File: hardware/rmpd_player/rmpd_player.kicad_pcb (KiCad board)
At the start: 2 copper layers, 108.6 x 69.2 mm, 117 parts, among them J1 POWER, J2 PROG, J3 LINE_OUT_INT_1, J4 LINE_OUT, J5 MICRO_SD, J6 POWER_INT, J7 LINE_OUT_INT_2, J8 RESERV, Q1 BC848, Q2 BC848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

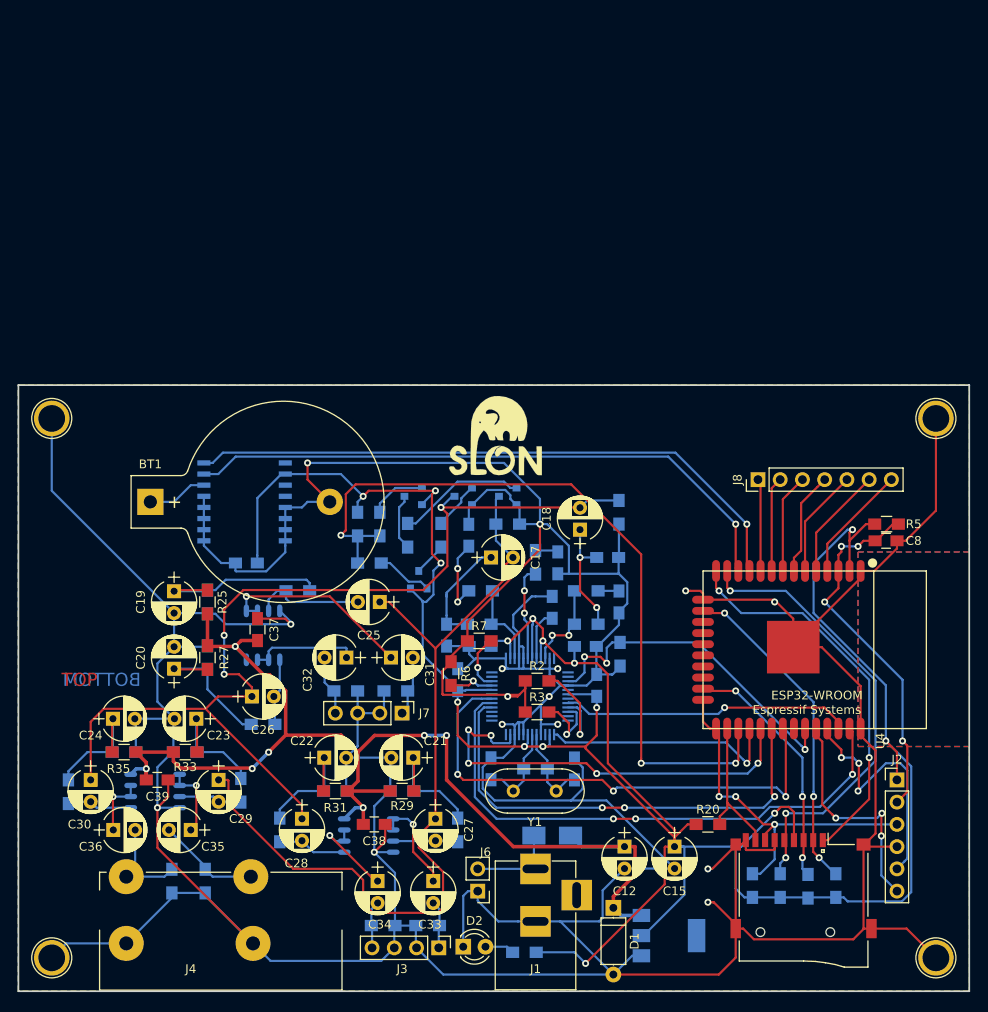
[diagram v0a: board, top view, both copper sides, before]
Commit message: smaller pcb
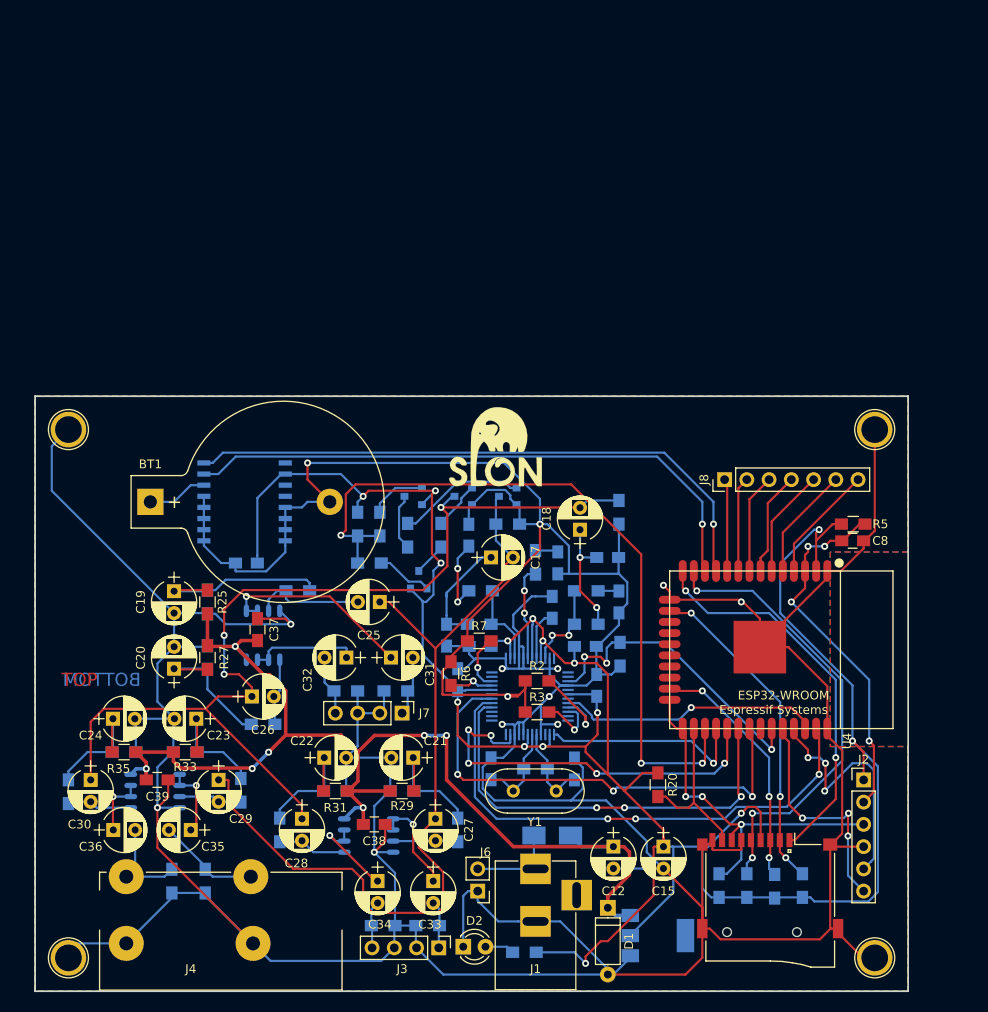
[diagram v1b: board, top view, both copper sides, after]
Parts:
- removed the REF** at (139.7, 76.2)
- removed the REF** at (139.7, 137.8)
- removed the REF** at (38.7, 76.2)
- added REF**: 1pin, Connectors:1pin, F.Cu at (132.7, 77.5)
- added REF**: 1pin, Connectors:1pin, F.Cu at (132.7, 137.8)
- added REF**: 1pin, Connectors:1pin, F.Cu at (40.6, 77.5)
- moved R20 7.29 mm to (108.0, 118.0), turned to 270 degrees
- moved R15 3.81 mm to (124.5, 129.5)
- moved C8 3.81 mm to (130.2, 90.2)
- moved J2 3.81 mm to (131.4, 117.5)
- moved J5 3.81 mm to (120.8, 134.9)
- moved J8 3.81 mm to (115.6, 83.2)
- moved R16 3.81 mm to (121.3, 129.6)
- moved R17 3.81 mm to (118.1, 129.5)
- moved R19 3.81 mm to (114.9, 129.5)
- moved R5 3.81 mm to (130.3, 88.3)
- moved U4 3.81 mm to (122.0, 102.6)
- moved REF** 1.91 mm to (40.6, 137.8)
- moved C15 1.27 mm to (108.6, 125.1)
- moved C12 1.27 mm to (102.9, 125.1)
- moved G*** 1.27 mm to (89.5, 79.4)
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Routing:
- net GND: track 706.3 -> 682.9 mm, vias 15 -> 13
- net VDD: track 314.8 -> 301.7 mm
- net VS_SI: track 63.8 -> 60.0 mm
- net VS_XCS: track 48.6 -> 44.8 mm
- net VS_SO: track 58.3 -> 54.5 mm
- net VS_SCLK: track 53.6 -> 49.8 mm
- net VS_XRESET: track 39.0 -> 35.2 mm
- net VS_XDCS: track 27.4 -> 23.6 mm
- net TRANSIENT_MUTE: track 88.7 -> 84.9 mm
- net VS_DREQ: track 33.2 -> 30.0 mm
- net 5V: track 137.2 -> 134.3 mm
- net Net-(R2-Pad2): track 12.4 -> 10.1 mm
- net I2C_SDA: track 70.2 -> 67.9 mm
- net I2C_SCL: track 71.3 -> 69.0 mm
- net SD_D1: track 17.4 -> 19.4 mm
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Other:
- board size 108.6 x 69.2 mm -> 99.7 x 67.9 mm

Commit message: better vdd route to ds3231
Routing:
- net VDD: track 301.7 -> 352.5 mm, vias 15 -> 17
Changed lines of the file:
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@@
-(kicad_pcb (version 20171130) (host pcbnew 5.0.1-5.0.1)
+(kicad_pcb (version 20171130) (host pcbnew 5.0.2-5.0.2)
   (general
     (thickness 1.6)
     (drawings 10)
-    (tracks 1084)
+    (tracks 1091)
     (zones 0)
     (modules 117)
@@
   (segment (start 128.905 88.265) (end 127.905 88.265) (width 0.25) (layer F.Cu) (net 5) (status 10))
   (segment (start 129.005 88.265) (end 128.905 88.265) (width 0.25) (layer F.Cu) (net 5) (status 30))
-  (segment (start 71.755 82.55) (end 74.295 85.09) (width 0.25) (layer B.Cu) (net 5))
   (segment (start 65.405 82.55) (end 71.755 82.55) (width 0.25) (layer B.Cu) (net 5) (status 10))
   (segment (start 114.035 130.89) (end 113.03 129.885) (width 0.25) (layer B.Cu) (net 5))
@@
   (segment (start 101.061501 112.298499) (end 101.061501 110.369868) (width 0.25) (layer F.Cu) (net 5))
   (segment (start 100.965 109.707682) (end 101.061501 109.804183) (width 0.25) (layer B.Cu) (net 5))
+  (via (at 89.535 82.55) (size 0.8) (drill 0.4) (layers F.Cu B.Cu) (net 5))
+  (segment (start 71.755 82.55) (end 89.535 82.55) (width 0.25) (layer B.Cu) (net 5))
+  (via (at 93.98 82.55) (size 0.8) (drill 0.4) (layers F.Cu B.Cu) (net 5))
+  (segment (start 89.535 82.55) (end 93.98 82.55) (width 0.25) (layer F.Cu) (net 5))
+  (segment (start 102.475002 82.55) (end 112.635002 92.71) (width 0.25) (layer B.Cu) (net 5))
+  (segment (start 93.98 82.55) (end 102.475002 82.55) (width 0.25) (layer B.Cu) (net 5))
+  (segment (start 121.850685 92.71) (end 121.92 92.779315) (width 0.25) (layer B.Cu) (net 5))
+  (segment (start 112.635002 92.71) (end 121.850685 92.71) (width 0.25) (layer B.Cu) (net 5))
   (segment (start 129.07 90.17) (end 128.945 90.17) (width 0.25) (layer F.Cu) (net 6) (status 30))
   (segment (start 130.975 88.265) (end 129.07 90.17) (width 0.25) (layer F.Cu) (net 6) (status 30))
@@
     (connect_pads (clearance 0.508))
     (min_thickness 0.254)
-    (fill (arc_segments 16) (thermal_gap 0.508) (thermal_bridge_width 0.508))
+    (fill yes (arc_segments 16) (thermal_gap 0.508) (thermal_bridge_width 0.508))
     (polygon
       (pts
@@
     (connect_pads (clearance 0.508))
     (min_thickness 0.254)
-    (fill (arc_segments 16) (thermal_gap 0.508) (thermal_bridge_width 0.508))
+    (fill yes (arc_segments 16) (thermal_gap 0.508) (thermal_bridge_width 0.508))
     (polygon
       (pts

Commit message: wip: volume control
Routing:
- net VDD: track 352.5 -> 354.7 mm
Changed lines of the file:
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@@
     (thickness 1.6)
     (drawings 10)
-    (tracks 1091)
+    (tracks 1096)
     (zones 0)
     (modules 117)
@@
   (segment (start 107.459999 125.170001) (end 107.535 125.095) (width 0.25) (layer F.Cu) (net 5))
   (segment (start 107.459999 130.665001) (end 107.459999 125.170001) (width 0.25) (layer F.Cu) (net 5))
-  (segment (start 109.710001 125.170001) (end 109.635 125.095) (width 0.25) (layer B.Cu) (net 5))
-  (segment (start 109.710001 130.319999) (end 109.710001 125.170001) (width 0.25) (layer B.Cu) (net 5))
-  (segment (start 109.635 125.095) (end 108.585 125.095) (width 0.25) (layer B.Cu) (net 5))
+  (segment (start 109.635 125.095) (end 108.585 125.095) (width 0.6) (layer B.Cu) (net 5))
   (segment (start 105.05 135.255) (end 105.05 134.98) (width 0.25) (layer B.Cu) (net 5))
-  (segment (start 105.05 134.98) (end 109.710001 130.319999) (width 0.25) (layer B.Cu) (net 5))
   (segment (start 99.695 114.3) (end 102.235 116.84) (width 0.25) (layer F.Cu) (net 5))
   (segment (start 99.695 113.665) (end 99.695 114.3) (width 0.25) (layer F.Cu) (net 5))
@@
   (segment (start 102.235 116.84) (end 104.14 118.745) (width 0.25) (layer F.Cu) (net 5))
   (segment (start 104.14 118.745) (end 108.585 123.19) (width 0.25) (layer F.Cu) (net 5))
-  (segment (start 113.03 125.095) (end 109.635 125.095) (width 0.25) (layer B.Cu) (net 5))
   (segment (start 101.061501 110.369868) (end 101.061501 109.804183) (width 0.25) (layer F.Cu) (net 5))
   (segment (start 99.695 113.665) (end 101.061501 112.298499) (width 0.25) (layer F.Cu) (net 5))
@@
   (segment (start 121.850685 92.71) (end 121.92 92.779315) (width 0.25) (layer B.Cu) (net 5))
   (segment (start 112.635002 92.71) (end 121.850685 92.71) (width 0.25) (layer B.Cu) (net 5))
+  (segment (start 104.8 135.255) (end 105.05 135.255) (width 0.25) (layer B.Cu) (net 5))
+  (segment (start 105.05 135.255) (end 107.315 135.255) (width 0.6) (layer B.Cu) (net 5))
+  (segment (start 107.315 135.255) (end 109.22 133.35) (width 0.6) (layer B.Cu) (net 5))
+  (segment (start 109.22 133.35) (end 109.22 131.445) (width 0.6) (layer B.Cu) (net 5))
+  (segment (start 109.22 131.445) (end 110.49 130.175) (width 0.6) (layer B.Cu) (net 5))
+  (segment (start 110.49 130.175) (end 110.49 125.95) (width 0.6) (layer B.Cu) (net 5))
+  (segment (start 110.49 125.95) (end 110.49 125.095) (width 0.6) (layer B.Cu) (net 5))
+  (segment (start 113.03 125.095) (end 110.49 125.095) (width 0.25) (layer B.Cu) (net 5))
+  (segment (start 110.49 125.095) (end 109.635 125.095) (width 0.6) (layer B.Cu) (net 5))
   (segment (start 129.07 90.17) (end 128.945 90.17) (width 0.25) (layer F.Cu) (net 6) (status 30))
   (segment (start 130.975 88.265) (end 129.07 90.17) (width 0.25) (layer F.Cu) (net 6) (status 30))
@@
   (segment (start 87.85 92.075) (end 83.82 96.105) (width 0.25) (layer B.Cu) (net 12))
   (segment (start 93.795 127.45) (end 93.98 127.635) (width 0.25) (layer B.Cu) (net 13) (status 30))
-  (segment (start 93.795 123.825) (end 93.795 127.45) (width 0.25) (layer B.Cu) (net 13) (status 30))
-  (segment (start 87.376 127.635) (end 93.98 127.635) (width 0.25) (layer B.Cu) (net 13))
+  (segment (start 93.795 123.825) (end 93.795 127.45) (width 0.8) (layer B.Cu) (net 13) (status 30))
+  (segment (start 87.376 127.635) (end 93.98 127.635) (width 0.8) (layer B.Cu) (net 13))
   (via (at 124.46 121.83) (size 0.8) (drill 0.4) (layers F.Cu B.Cu) (net 14))
   (via (at 129.660748 123.877066) (size 0.8) (drill 0.4) (layers F.Cu B.Cu) (net 14))
@@
   (segment (start 81.28 112.395) (end 83.82 112.395) (width 0.4) (layer B.Cu) (net 55))
   (via (at 83.82 112.395) (size 0.8) (drill 0.4) (layers F.Cu B.Cu) (net 55))
-  (segment (start 103.11 132.955) (end 102.235 132.08) (width 0.4) (layer B.Cu) (net 55))
-  (segment (start 104.8 132.955) (end 103.11 132.955) (width 0.4) (layer B.Cu) (net 55))
-  (segment (start 102.235 130.78) (end 102.235 132.08) (width 0.4) (layer F.Cu) (net 55))
-  (segment (start 104.705001 128.309999) (end 102.235 130.78) (width 0.4) (layer F.Cu) (net 55))
-  (segment (start 104.07 125.095) (end 102.87 125.095) (width 0.4) (layer F.Cu) (net 55))
-  (segment (start 104.705001 125.730001) (end 104.07 125.095) (width 0.4) (layer F.Cu) (net 55))
-  (segment (start 104.705001 128.309999) (end 104.705001 125.730001) (width 0.4) (layer F.Cu) (net 55))
+  (segment (start 103.11 132.955) (end 102.235 132.08) (width 0.8) (layer B.Cu) (net 55))
+  (segment (start 104.8 132.955) (end 103.11 132.955) (width 0.8) (layer B.Cu) (net 55))
+  (segment (start 102.235 130.78) (end 102.235 132.08) (width 0.8) (layer F.Cu) (net 55))
+  (segment (start 104.705001 128.309999) (end 102.235 130.78) (width 0.8) (layer F.Cu) (net 55))
+  (segment (start 104.07 125.095) (end 102.87 125.095) (width 0.8) (layer F.Cu) (net 55))
+  (segment (start 104.705001 125.730001) (end 104.07 125.095) (width 0.8) (layer F.Cu) (net 55))
+  (segment (start 104.705001 128.309999) (end 104.705001 125.730001) (width 0.8) (layer F.Cu) (net 55))
   (segment (start 91.44 125.095) (end 102.87 125.095) (width 0.4) (layer F.Cu) (net 55))
   (segment (start 83.82 112.395) (end 83.82 117.475) (width 0.4) (layer F.Cu) (net 55))
   (segment (start 83.82 117.475) (end 91.44 125.095) (width 0.4) (layer F.Cu) (net 55))
-  (segment (start 99.245 125.095) (end 97.975 123.825) (width 0.4) (layer B.Cu) (net 55))
-  (segment (start 102.87 125.095) (end 99.245 125.095) (width 0.4) (layer B.Cu) (net 55))
+  (segment (start 99.245 125.095) (end 97.975 123.825) (width 0.8) (layer B.Cu) (net 55))
+  (segment (start 102.87 125.095) (end 99.245 125.095) (width 0.8) (layer B.Cu) (net 55))
   (segment (start 82.55 121.92) (end 82.55 102.455) (width 0.25) (layer F.Cu) (net 56) (status 10))
   (segment (start 89.495 88.305) (end 89.455 88.265) (width 0.25) (layer B.Cu) (net 56) (status 30))
@@
     (connect_pads (clearance 0.508))
     (min_thickness 0.254)
-    (fill yes (arc_segments 16) (thermal_gap 0.508) (thermal_bridge_width 0.508))
+    (fill (arc_segments 16) (thermal_gap 0.508) (thermal_bridge_width 0.508))
     (polygon
       (pts
@@
     (connect_pads (clearance 0.508))
     (min_thickness 0.254)
-    (fill yes (arc_segments 16) (thermal_gap 0.508) (thermal_bridge_width 0.508))
+    (fill (arc_segments 16) (thermal_gap 0.508) (thermal_bridge_width 0.508))
     (polygon
       (pts

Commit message: wip: new tps54331 power
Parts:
- added C40: 1000pF, Capacitors_SMD:C_0805_HandSoldering, F.Cu at (107.9, 139.1)
- added C41: 1000pF, Capacitors_SMD:C_0805_HandSoldering, F.Cu at (113.7, 43.4)
- added C42: 10.0, Capacitors_THT:CP_Radial_D5.0mm_P2.50mm, F.Cu at (101.6, 123.8)
- added C43: 10.0, Capacitors_THT:CP_Radial_D5.0mm_P2.50mm, F.Cu at (95.0, 35.3)
- added C44: 47pF, Capacitors_SMD:C_0805_HandSoldering, B.Cu at (111.8, 139.1)
- added C45: 47pF, Capacitors_SMD:C_0805_HandSoldering, F.Cu at (111.9, 45.9)
- added C46: 0.01, Capacitors_SMD:C_0805_HandSoldering, B.Cu at (109.2, 127.0)
- added C47: 0.01, Capacitors_SMD:C_0805_HandSoldering, F.Cu at (111.9, 47.7)
- added C48: 100n, Capacitors_SMD:C_0805_HandSoldering, F.Cu at (100.3, 135.3)
- added C49: 100n, Capacitors_SMD:C_0805_HandSoldering, F.Cu at (111.9, 49.5)
- added C50: 47uF, Capacitors_SMD:C_1206_HandSoldering, B.Cu at (116.1, 137.2)
- added C51: 47uF, Capacitors_SMD:C_1206_HandSoldering, F.Cu at (101.6, 48.2)
- added C52: 47uF, Capacitors_SMD:C_1206_HandSoldering, B.Cu at (122.5, 137.2)
- added C53: 47uF, Capacitors_SMD:C_1206_HandSoldering, F.Cu at (108.2, 43.9)
- added D3: B340, Opto-Devices:PhotoDiode_SMD-DIL2_4.5x4, F.Cu at (120.7, 37.5)
- added L1: 6.8uH, Inductors_SMD:L_6.3x6.3_H3, F.Cu at (104.8, 134.0)
- added L2: 6.8uH, Inductors_SMD:L_6.3x6.3_H3, F.Cu at (94.6, 44.1)
- added R50: 30k, Resistors_SMD:R_0805_HandSoldering, F.Cu at (102.9, 139.1)
- added R51: 30k, Resistors_SMD:R_0805_HandSoldering, F.Cu at (100.7, 52.1)
- added R52: 15k, Resistors_SMD:R_0805_HandSoldering, F.Cu at (111.1, 129.5)
- added R53: 4k7, Resistors_SMD:R_0805_HandSoldering, B.Cu at (111.1, 132.7)
- added R54: 10k, Resistors_SMD:R_0805_HandSoldering, F.Cu at (113.8, 41.6)
- added R55: 1k6, Resistors_SMD:R_0805_HandSoldering, F.Cu at (100.7, 50.2)
- added U8: TPS54331D, Housings_SOIC:SOIC-8_3.9x4.9mm_Pitch1.27mm, B.Cu at (106.0, 134.6)
- added U9: TPS54331D, Housings_SOIC:SOIC-8_3.9x4.9mm_Pitch1.27mm, F.Cu at (130.6, 63.1)
- C17: value 10.0 -> 0.01; footprint Capacitors_THT:CP_Radial_D5.0mm_P2.50mm -> Capacitors_SMD:C_0805_HandSoldering; moved to B.Cu
- C18: value 10.0 -> 0.01; footprint Capacitors_THT:CP_Radial_D5.0mm_P2.50mm -> Capacitors_SMD:C_0805_HandSoldering
- D1: value 5.1V -> B340; footprint Diodes_THT:D_A-405_P7.62mm_Horizontal -> Opto-Devices:PhotoDiode_SMD-DIL2_4.5x4
- R20: moved to B.Cu
- moved C12 76.3 mm to (76.8, 53.3)
- moved U3 75.7 mm to (83.8, 63.5)
- moved C15 75.1 mm to (70.5, 60.3)
- moved C18 60.7 mm to (135.9, 40.6), turned to 0 degrees
- moved C17 36.6 mm to (104.8, 125.1), turned to 270 degrees
- moved R20 19.1 mm to (119.3, 133.3), turned to 180 degrees
- moved D1 8.54 mm to (108.0, 125.7), turned to 90 degrees
- moved F1 6.63 mm to (90.2, 127.2), turned to 90 degrees
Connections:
- net Net-(F1-Pad1) renamed /VIN_UNFUSED
- C12 pad 1: 5V -> VDDA_OP
- C14 pad 2: Net-(C14-Pad2) -> OUT_L
- C15 pad 1: VDD -> VDDA_VS
- C16 pad 2: Net-(C16-Pad2) -> OUT_R
- C17 pad 1: Net-(C16-Pad2) -> VIN
- C17 pad 2: OUT_R -> GND
- C18 pad 1: Net-(C14-Pad2) -> VIN
- C18 pad 2: OUT_L -> GND
- C3 pad 2: VDD -> VDD_ESP
- C37 pad 1: 5V -> VDDA_OP
- C38 pad 1: 5V -> VDDA_OP
- C39 pad 1: 5V -> VDDA_OP
- C4 pad 1: VDD -> VDDA_VS
- C5 pad 1: VDD -> VDDA_VS
- C6 pad 1: VDD -> VDDA_VS
- C7 pad 1: VDD -> VDDA_VS
- D1 pad 1: 5V -> Net-(C48-Pad1)
- F1 pad 2: 5V -> VIN
- J2 pad 1: VDD -> VDD_ESP
- J5 pad 4: VDD -> VDD_ESP
- Q1 pad 3: OUT_R -> Net-(C36-Pad2)
- Q2 pad 3: OUT_L -> Net-(C35-Pad2)
- Q3 pad 2: VDD -> VDDA_VS
- Q4 pad 2: VDD -> VDDA_VS
- R11 pad 2: Net-(C16-Pad2) -> OUT_R
- R12 pad 2: Net-(C14-Pad2) -> OUT_L
- R15 pad 1: VDD -> VDD_ESP
- R16 pad 1: VDD -> VDD_ESP
- R17 pad 1: VDD -> VDD_ESP
- R19 pad 1: VDD -> VDD_ESP
- R20 pad 1: VDD -> VDD_ESP
- R24 pad 1: VDD -> VDDA_VS
- R25 pad 2: 5V -> VDDA_OP
- R27 pad 2: 5V -> VDDA_OP
- R29 pad 2: 5V -> VDDA_OP
- R31 pad 2: 5V -> VDDA_OP
- R33 pad 2: 5V -> VDDA_OP
- R35 pad 2: 5V -> VDDA_OP
- R49 pad 1: VDD -> VDD_ESP
- R5 pad 1: VDD -> VDD_ESP
- U1 pad 2: VDD -> VDD_ESP
- U2 pad 14: VDD -> VDDA_VS
- U2 pad 19: VDD -> VDDA_VS
- U2 pad 32: VDD -> VDDA_VS
- U2 pad 38: VDD -> VDDA_VS
- U2 pad 43: VDD -> VDDA_VS
- U2 pad 45: VDD -> VDDA_VS
- U2 pad 6: VDD -> VDDA_VS
- U3 pad 2: VDD -> VDDA_VS
- U3 pad 3: 5V -> VDDA_OP
- U4 pad 2: VDD -> VDD_ESP
- U5 pad 8: 5V -> VDDA_OP
- U6 pad 8: 5V -> VDDA_OP
- U7 pad 8: 5V -> VDDA_OP
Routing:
- net VDD: track 354.7 -> 0.00 mm, vias 17 -> 0
- net 5V: track 134.3 -> 0.00 mm, vias 7 -> 0
- net VDD_ESP: track 0.00 -> 96.4 mm, vias 0 -> 2
- net VDDA_OP: track 0.00 -> 75.1 mm, vias 0 -> 6
- net VS_SI: track 60.0 -> 0.00 mm, vias 3 -> 0
- net VS_SO: track 54.5 -> 0.00 mm, vias 3 -> 0
- net VS_SCLK: track 49.8 -> 0.00 mm, vias 3 -> 0
- net VS_XCS: track 44.8 -> 0.00 mm, vias 5 -> 0
- net GND: track 682.9 -> 714.1 mm, vias 13 -> 29
- net VIN: track 0.00 -> 29.6 mm
- net Net-(C48-Pad1): track 0.00 -> 23.1 mm, vias 0 -> 1
- net Net-(C40-Pad1): track 0.00 -> 13.8 mm, vias 0 -> 1
- net Net-(C14-Pad2): track 13.6 -> 0.00 mm, vias 2 -> 0
- net OUT_L: track 112.9 -> 126.5 mm, vias 3 -> 5
- net Net-(C16-Pad2): track 12.9 -> 0.00 mm
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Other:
- net class input power added: clearance 0.3, trace_width 1.2, via_dia 1.5, via_drill 0.8
- net class power: trace_width 0.4 -> 0.35; via_dia 0.8 -> 1; via_drill 0.4 -> 0.6

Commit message: new pcb
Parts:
- C18, C45, C47, C51, C53, C8, R5, R51, R54, R55: moved to B.Cu
- moved C43 53.6 mm to (116.2, 84.5)
- moved C18 45.2 mm to (117.5, 81.9)
- moved R51 45.1 mm to (132.1, 84.5), turned to 270 degrees
- moved C41 44.9 mm to (132.1, 84.5), turned to 270 degrees
- moved R54 41.9 mm to (127.0, 81.4), turned to 90 degrees
- moved L2 40.3 mm to (116.2, 78.1)
- moved D3 40.2 mm to (124.5, 77.5)
- moved C47 40.0 mm to (113.0, 87.6), turned to 180 degrees
- moved C45 37.4 mm to (123.8, 81.3), turned to 90 degrees
- moved R55 36.1 mm to (125.8, 76.2)
- moved C49 34.4 mm to (109.9, 83.8)
- moved C53 34.2 mm to (107.3, 78.1), turned to 270 degrees
- moved C12 34.2 mm to (102.2, 76.2)
- moved C51 30.9 mm to (109.9, 78.0), turned to 270 degrees
- moved U9 20.5 mm to (124.5, 82.5)
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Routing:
- net GND: track 714.1 -> 926.2 mm, vias 29 -> 57
- net VDD_ESP: track 96.4 -> 300.4 mm, vias 2 -> 6
- net VDDA_VS: track 0.00 -> 192.3 mm, vias 0 -> 14
- net VDDA_OP: track 75.1 -> 233.8 mm, vias 6 -> 10
- net Net-(C36-Pad2): track 11.3 -> 109.9 mm, vias 0 -> 2
- net Net-(C35-Pad2): track 11.8 -> 109.9 mm, vias 0 -> 2
- net VIN: track 29.6 -> 98.8 mm, vias 0 -> 1
- net VS_SI: track 0.00 -> 60.0 mm, vias 0 -> 3
- net VS_SO: track 0.00 -> 48.5 mm, vias 0 -> 3
- net VS_SCLK: track 0.00 -> 42.8 mm, vias 0 -> 5
- net VS_XCS: track 0.00 -> 31.1 mm, vias 0 -> 3
- net Net-(C49-Pad1): track 0.00 -> 26.6 mm
- net Net-(R54-Pad1): track 0.00 -> 12.3 mm, vias 0 -> 1
- net Net-(C49-Pad2): track 0.00 -> 12.3 mm
- net Net-(C41-Pad1): track 0.00 -> 9.99 mm, vias 0 -> 1
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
